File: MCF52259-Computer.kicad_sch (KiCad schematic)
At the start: 4 parts, among them Y1 8MHz

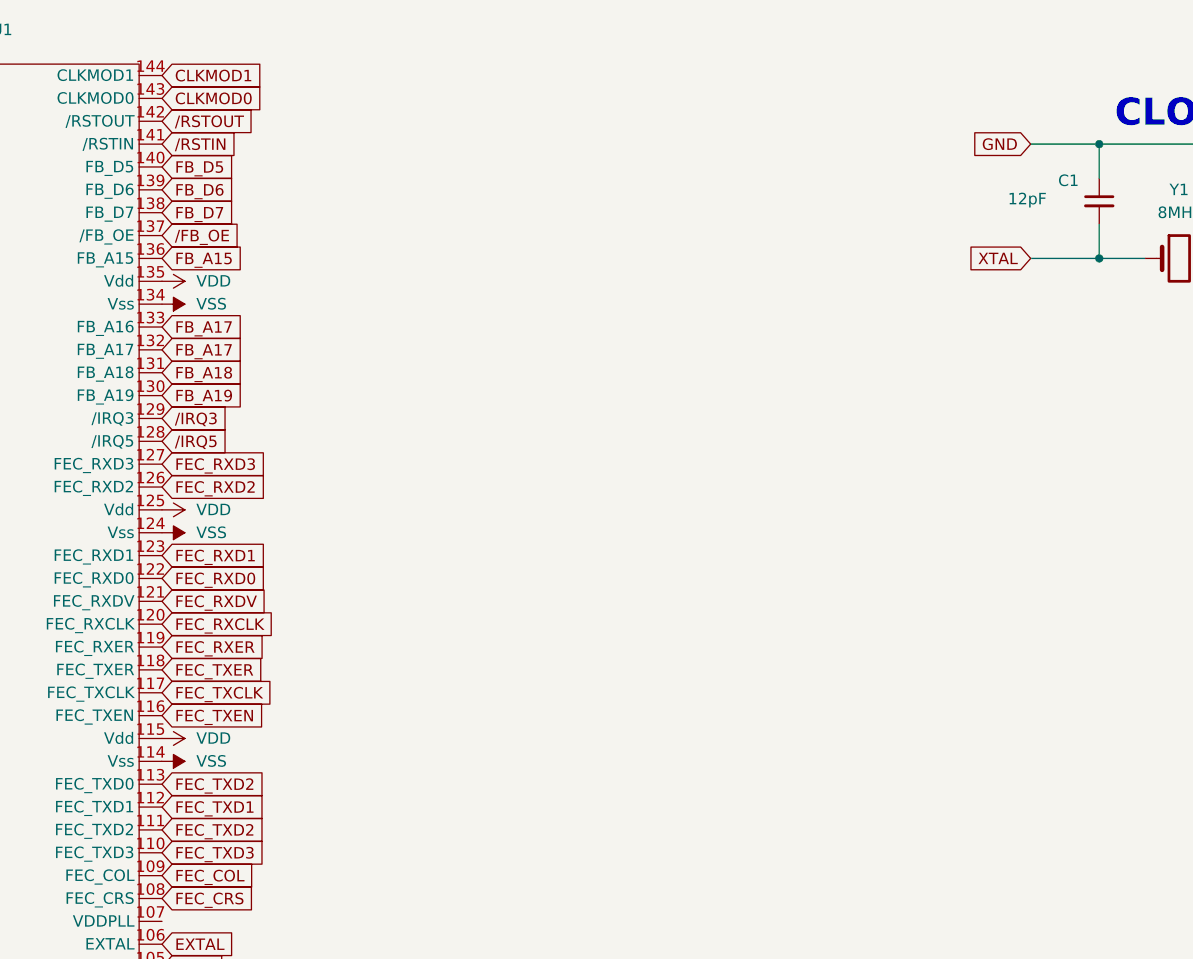
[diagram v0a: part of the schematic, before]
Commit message: Configured Clock Modes Correctly
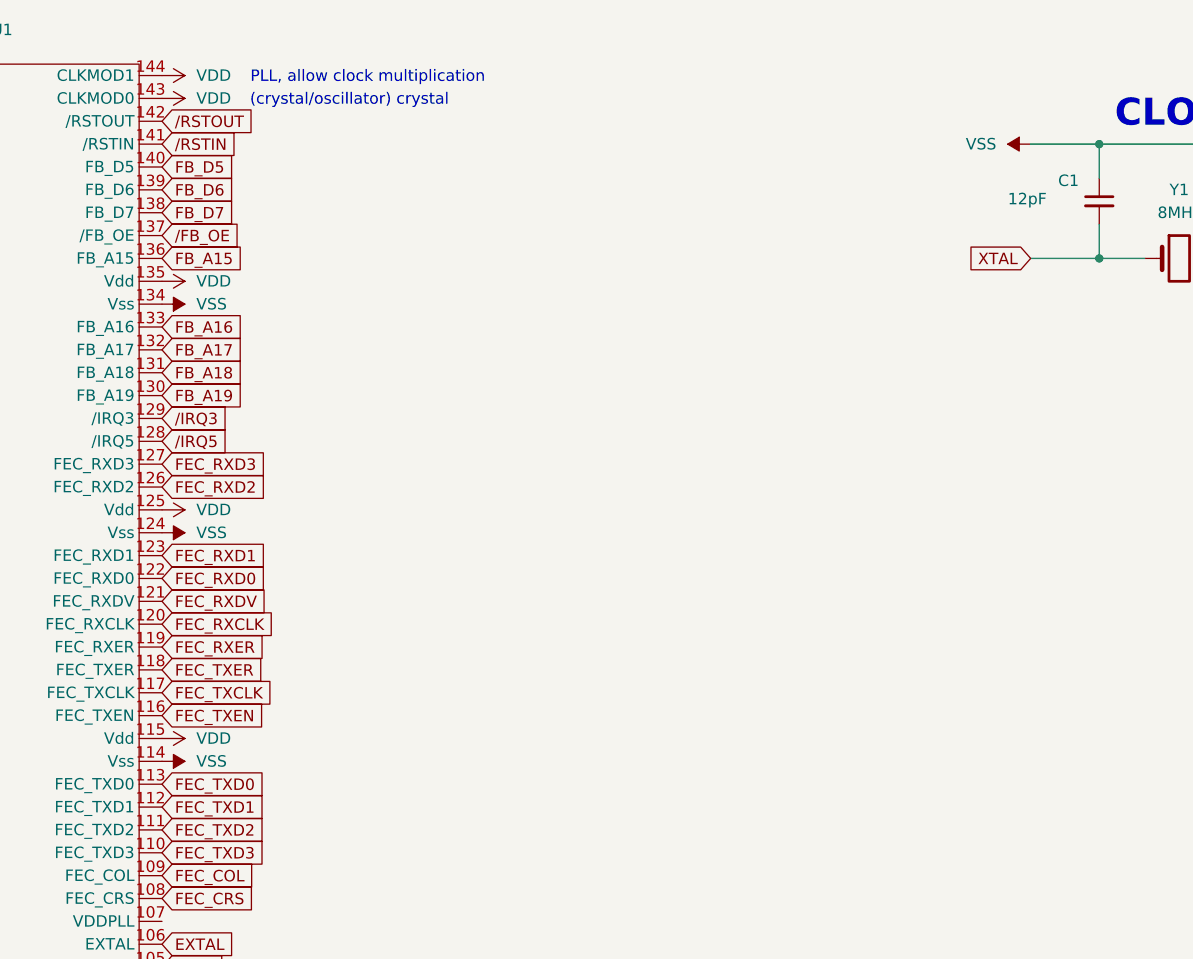
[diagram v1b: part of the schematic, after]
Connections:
- net CLKMOD0 is gone; now on net VDD: U1.143 (CLKMOD0)
- net CLKMOD1 is gone; now on net VDD: U1.144 (CLKMOD1)
- net GND is gone; now on net VSS: C1.1, C2.1
- net FB_A17: no longer U1.133 (FB_A16)
- net FEC_TXD2: no longer U1.113 (FEC_TXD0)
- new net FB_A16: U1.133 (FB_A16)
- new net FEC_TXD0: U1.113 (FEC_TXD0)
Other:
- note added: "(crystal/oscillator) crystal"
- note added: "PLL, allow clock multiplication"
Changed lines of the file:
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@@
 		)
 	)
+	(text "(crystal/oscillator) crystal"
+		(exclude_from_sim no)
+		(at 104.648 18.034 0)
+		(effects
+			(font
+				(size 1.27 1.27)
+			)
+		)
+	)
+	(text "PLL, allow clock multiplication"
+		(exclude_from_sim no)
+		(at 106.68 15.494 0)
+		(effects
+			(font
+				(size 1.27 1.27)
+			)
+		)
+	)
 	(junction
 		(at 187.96 22.86)
@@
 		)
 	)
-	(global_label "CLKMOD0"
-		(shape input)
-		(at 83.82 17.78 0)
-		(fields_autoplaced yes)
-		(effects
-			(font
-				(size 1.27 1.27)
-			)
-			(justify left)
-		)
-		(property "Intersheetrefs" "${INTERSHEET_REFS}"
-			(at 95.6347 17.78 0)
-			(effects
-				(font
-					(size 1.27 1.27)
-				)
-				(justify left)
-				(hide yes)
-			)
-		)
-	)
 	(global_label "FB_D3"
 		(shape input)
@@
 		)
 	)
-	(global_label "FB_A17"
+	(global_label "FB_A16"
 		(shape input)
 		(at 83.82 43.18 0)
@@
 		)
 	)
-	(global_label "CLKMOD1"
-		(shape input)
-		(at 83.82 15.24 0)
-		(fields_autoplaced yes)
-		(effects
-			(font
-				(size 1.27 1.27)
-			)
-			(justify left)
-		)
-		(property "Intersheetrefs" "${INTERSHEET_REFS}"
-			(at 95.6347 15.24 0)
-			(effects
-				(font
-					(size 1.27 1.27)
-				)
-				(justify left)
-				(hide yes)
-			)
-		)
-	)
 	(global_label "ICOC0"
 		(shape input)
@@
 		)
 	)
-	(global_label "FEC_TXD2"
+	(global_label "FEC_TXD0"
 		(shape input)
 		(at 83.82 93.98 0)
@@
 		)
 	)
-	(global_label "GND"
-		(shape input)
-		(at 180.34 22.86 180)
-		(fields_autoplaced yes)
-		(effects
-			(font
-				(size 1.27 1.27)
-			)
-			(justify right)
-		)
-		(property "Intersheetrefs" "${INTERSHEET_REFS}"
-			(at 173.4843 22.86 0)
-			(effects
-				(font
-					(size 1.27 1.27)
-				)
-				(justify right)
-				(hide yes)
-			)
-		)
-	)
 	(global_label "FB_A11"
 		(shape input)
@@
 	(symbol
 		(lib_id "power:VDD")
+		(at 83.82 15.24 270)
+		(unit 1)
+		(exclude_from_sim no)
+		(in_bom yes)
+		(on_board yes)
+		(dnp no)
+		(fields_autoplaced yes)
+		(property "Reference" "#PWR022"
+			(at 80.01 15.24 0)
+			(effects
+				(font
+					(size 1.27 1.27)
+				)
+				(hide yes)
+			)
+		)
+		(property "Value" "VDD"
+			(at 87.63 15.2399 90)
+			(effects
+				(font
+					(size 1.27 1.27)
+				)
+				(justify left)
+			)
+		)
+		(property "Footprint" ""
+			(at 83.82 15.24 0)
+			(effects
+				(font
+					(size 1.27 1.27)
+				)
+				(hide yes)
+			)
+		)
+		(property "Datasheet" ""
+			(at 83.82 15.24 0)
+			(effects
+				(font
+					(size 1.27 1.27)
+				)
+				(hide yes)
+			)
+		)
+		(property "Description" "Power symbol creates a global label with name \"VDD\""
+			(at 83.82 15.24 0)
+			(effects
+				(font
+					(size 1.27 1.27)
+				)
+				(hide yes)
+			)
+		)
+		(pin "1"
+		)
+		(instances
+			(project "MCF52259-Computer"
+				(path "/c15ade3d-bb7e-4014-8f2f-451af952ec03"
+					(reference "#PWR022")
+					(unit 1)
+				)
+			)
+		)
+	)
+	(symbol
+		(lib_id "power:VDD")
 		(at 48.26 30.48 90)
 		(unit 1)
@@
 	)
 	(symbol
+		(lib_id "power:VSS")
+		(at 180.34 22.86 90)
+		(unit 1)
+		(exclude_from_sim no)
+		(in_bom yes)
+		(on_board yes)
+		(dnp no)
+		(fields_autoplaced yes)
+		(property "Reference" "#PWR021"
+			(at 184.15 22.86 0)
+			(effects
+				(font
+					(size 1.27 1.27)
+				)
+				(hide yes)
+			)
+		)
+		(property "Value" "VSS"
+			(at 176.53 22.8599 90)
+			(effects
+				(font
+					(size 1.27 1.27)
+				)
+				(justify left)
+			)
+		)
+		(property "Footprint" ""
+			(at 180.34 22.86 0)
+			(effects
+				(font
+					(size 1.27 1.27)
+				)
+				(hide yes)
+			)
+		)
+		(property "Datasheet" ""
+			(at 180.34 22.86 0)
+			(effects
+				(font
+					(size 1.27 1.27)
+				)
+				(hide yes)
+			)
+		)
+		(property "Description" "Power symbol creates a global label with name \"VSS\""
+			(at 180.34 22.86 0)
+			(effects
+				(font
+					(size 1.27 1.27)
+				)
+				(hide yes)
+			)
+		)
+		(pin "1"
+		)
+		(instances
+			(project "MCF52259-Computer"
+				(path "/c15ade3d-bb7e-4014-8f2f-451af952ec03"
+					(reference "#PWR021")
+					(unit 1)
+				)
+			)
+		)
+	)
+	(symbol
 		(lib_id "power:VDD")
 		(at 48.26 162.56 90)
@@
 					(unit 1)
 				)
+			)
+		)
+	)
+	(symbol
+		(lib_id "power:VDD")
+		(at 83.82 17.78 270)
+		(unit 1)
+		(exclude_from_sim no)
+		(in_bom yes)
+		(on_board yes)
+		(dnp no)
+		(fields_autoplaced yes)
+		(property "Reference" "#PWR023"
+			(at 80.01 17.78 0)
+			(effects
+				(font
+					(size 1.27 1.27)
+				)
+				(hide yes)
+			)
+		)
+		(property "Value" "VDD"
+			(at 87.63 17.7799 90)
+			(effects
+				(font
+					(size 1.27 1.27)
+				)
+				(justify left)
+			)
+		)
+		(property "Footprint" ""
+			(at 83.82 17.78 0)
+			(effects
+				(font
+					(size 1.27 1.27)
+				)
+				(hide yes)
+			)
+		)
+		(property "Datasheet" ""
+			(at 83.82 17.78 0)
+			(effects
+				(font
+					(size 1.27 1.27)
+				)
+				(hide yes)
+			)
+		)
+		(property "Description" "Power symbol creates a global label with name \"VDD\""
+			(at 83.82 17.78 0)
+			(effects
+				(font
+					(size 1.27 1.27)
+				)
+				(hide yes)
+			)
+		)
+		(pin "1"
+		)
+		(instances
+			(project "MCF52259-Computer"
+				(path "/c15ade3d-bb7e-4014-8f2f-451af952ec03"
+					(reference "#PWR023")
+					(unit 1)
+				)

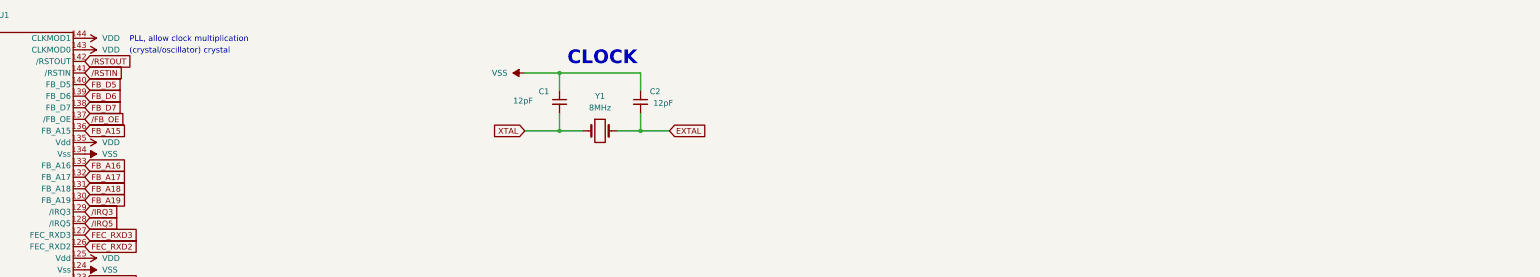
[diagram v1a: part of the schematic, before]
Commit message: Added Reset Circuitry
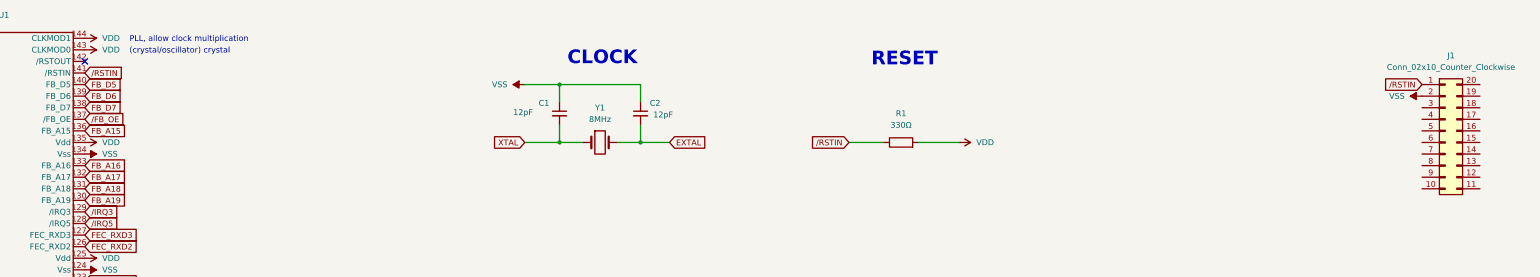
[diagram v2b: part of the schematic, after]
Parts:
- added J1: Conn_02x10_Counter_Clockwise, Connector_PinHeader_2.54mm:PinHeader_2x10_P2.54mm_Vertical, symbol Connector_Generic:Conn_02x10_Counter_Clockwise
- added R1: 330Ω, Resistor_SMD:R_0805_2012Metric_Pad1.20x1.40mm_HandSolder, symbol Device:R
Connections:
- net VDD: now also R1.2
- net VSS: now also J1.2 (Pin_2)
- net /RSTIN: now also J1.1 (Pin_1), R1.1
- net /RSTOUT: no longer names the net of U1.142 (/RSTOUT)
- no-connect marks 0 -> 1
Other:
- note added: "RESET"
- moved on the sheet: C1, C2, Y1

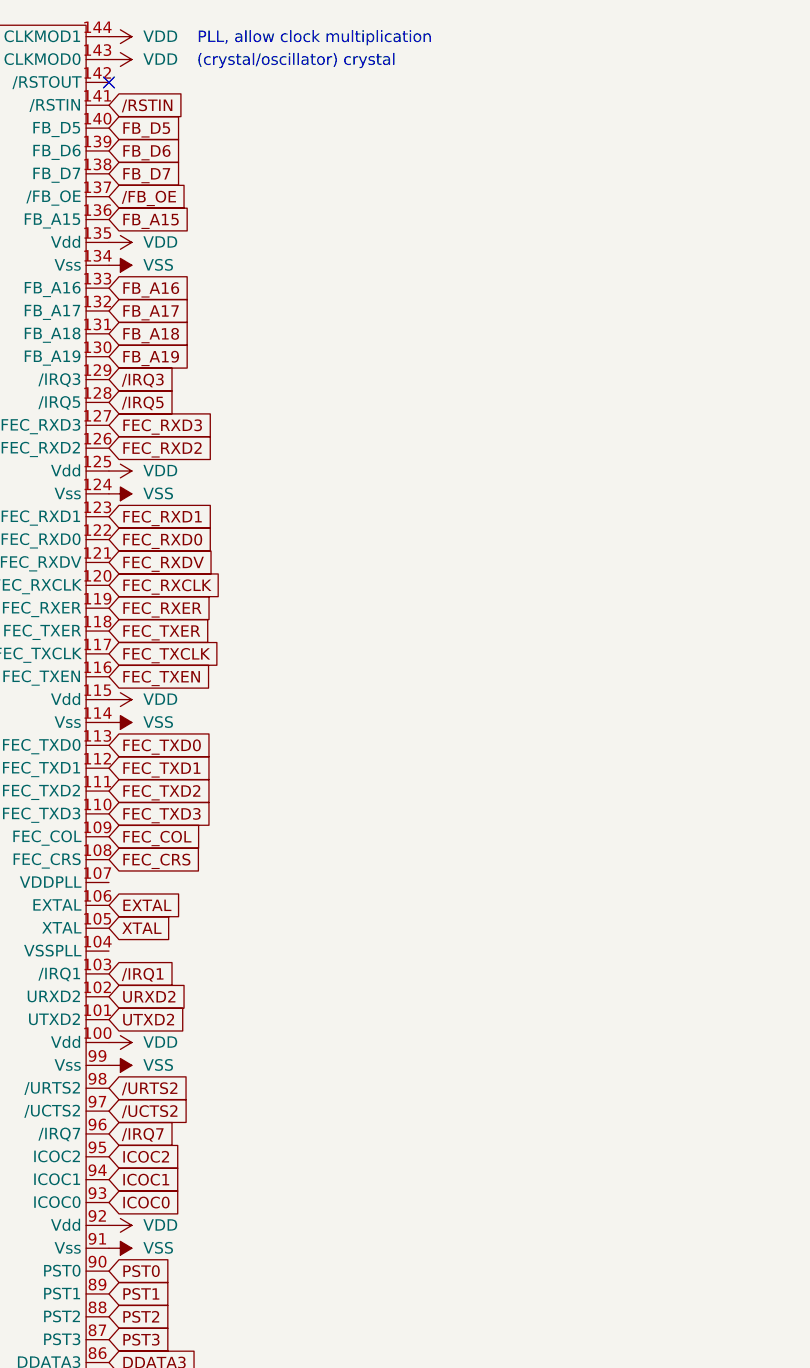
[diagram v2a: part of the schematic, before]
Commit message: Added Decoupling Caps
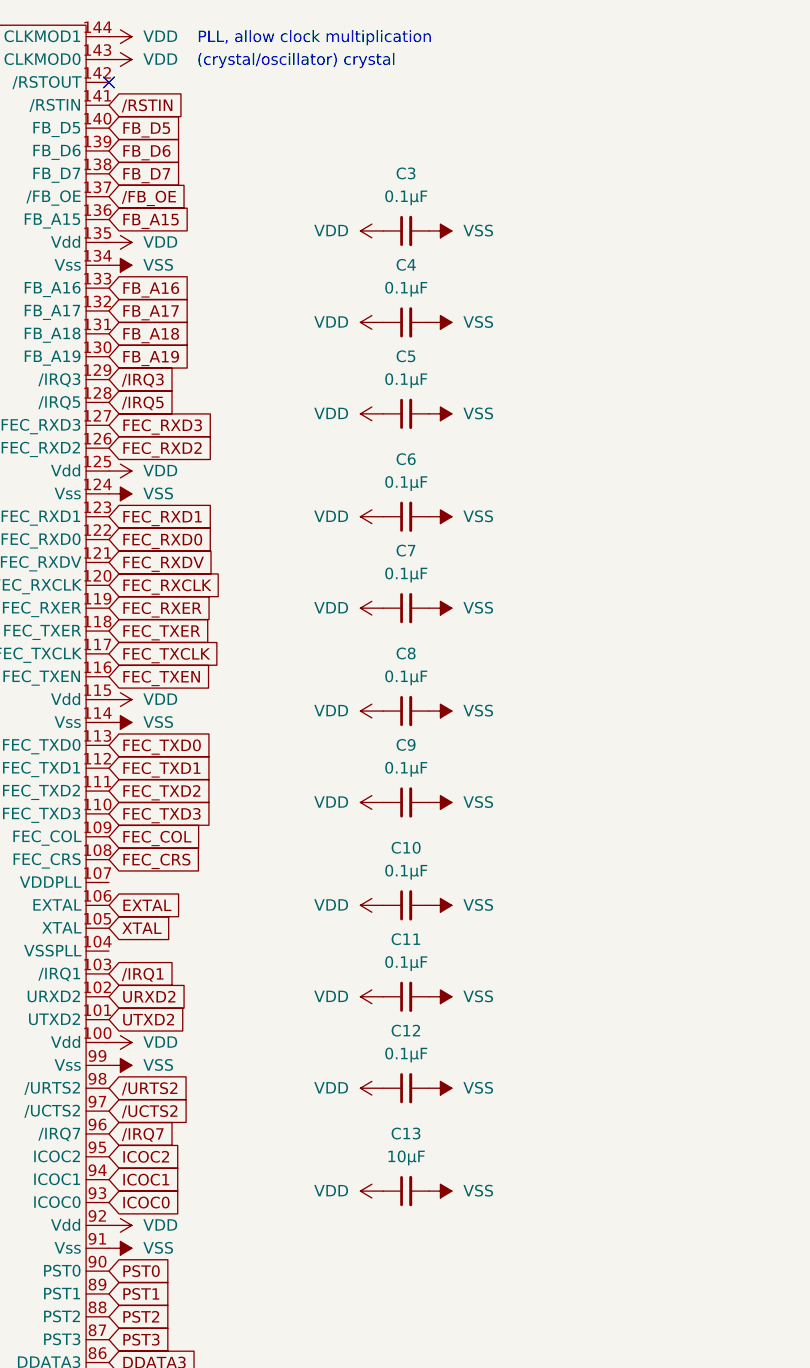
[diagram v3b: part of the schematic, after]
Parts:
- added C10, C11, C12, C3, C4, C5, C6, C7, C8, C9: 0.1µF, Capacitor_SMD:C_0805_2012Metric_Pad1.18x1.45mm_HandSolder, symbol Device:C_Small
- added C13: 10µF, Capacitor_SMD:C_0603_1608Metric_Pad1.08x0.95mm_HandSolder, symbol Device:C_Small
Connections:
- net VDD: now also C10.1, C11.1, C12.1, C13.1, C3.1, C4.1, C5.1, C6.1, C7.1, C8.1, C9.1
- net VSS: now also C10.2, C11.2, C12.2, C13.2, C3.2, C4.2, C5.2, C6.2, C7.2, C8.2, C9.2
